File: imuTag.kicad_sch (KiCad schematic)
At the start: 29 parts, among them J1 Conn_02x05_Odd_Even, J2 Conn_01x05_Socket, J3 Conn_01x02_Pin, U1 E73-2G4M08S1C, U2 ME6211C30M5G-N, U3 GD25Q64ESIG, Y2 Crystal

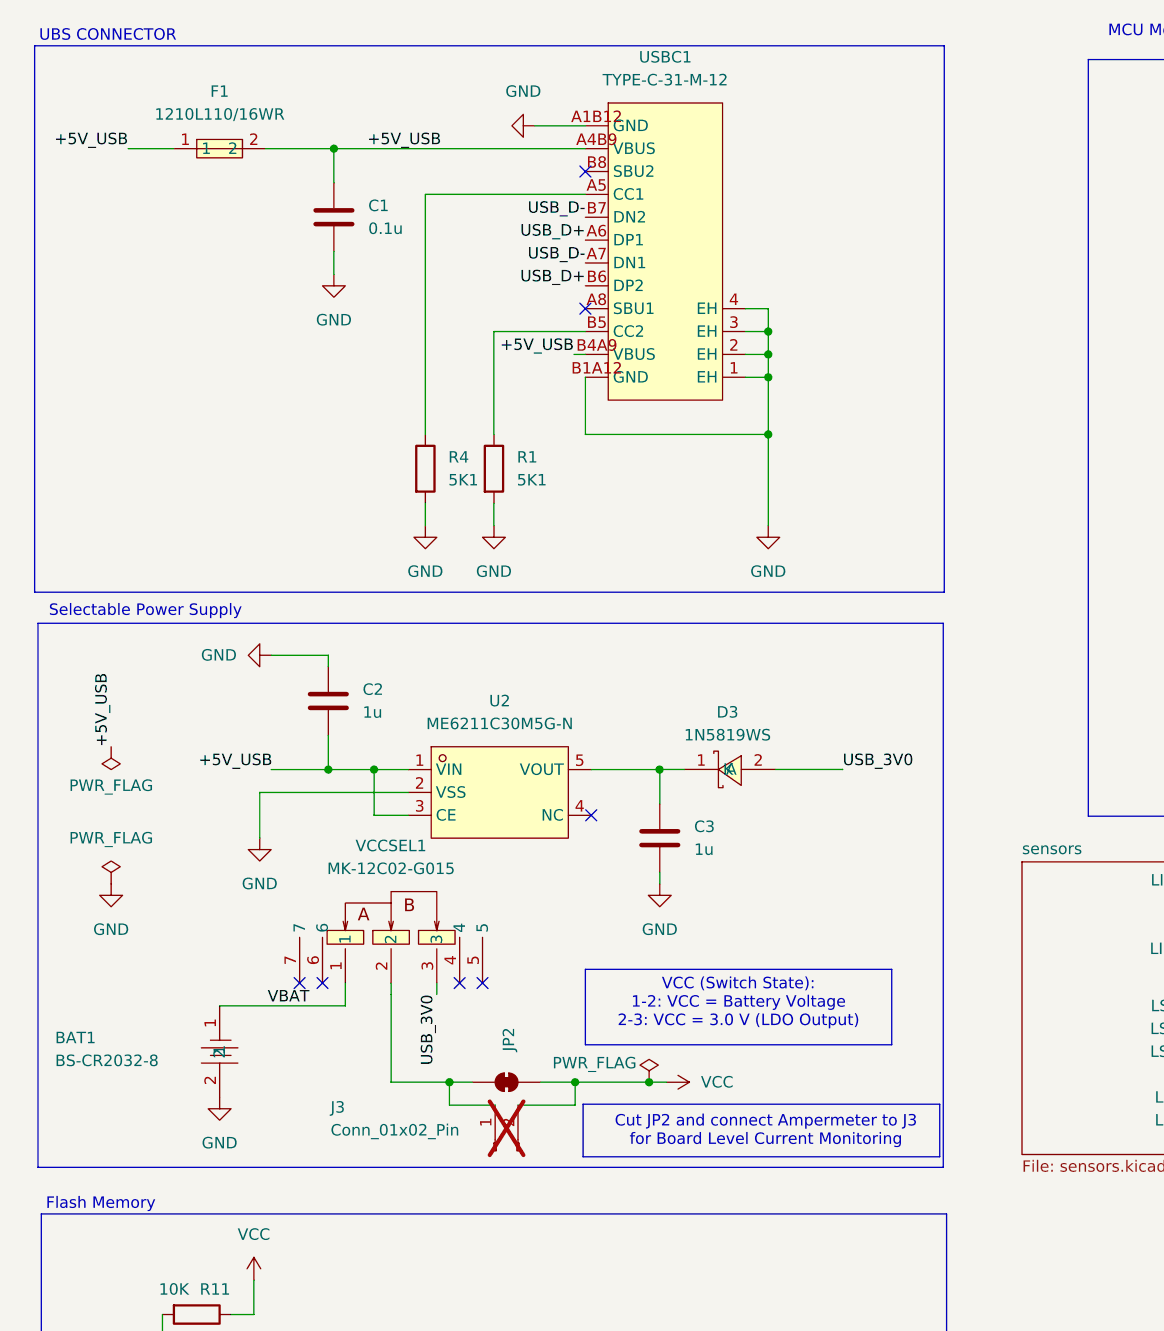
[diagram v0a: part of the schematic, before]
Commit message: Add copper zones before routing
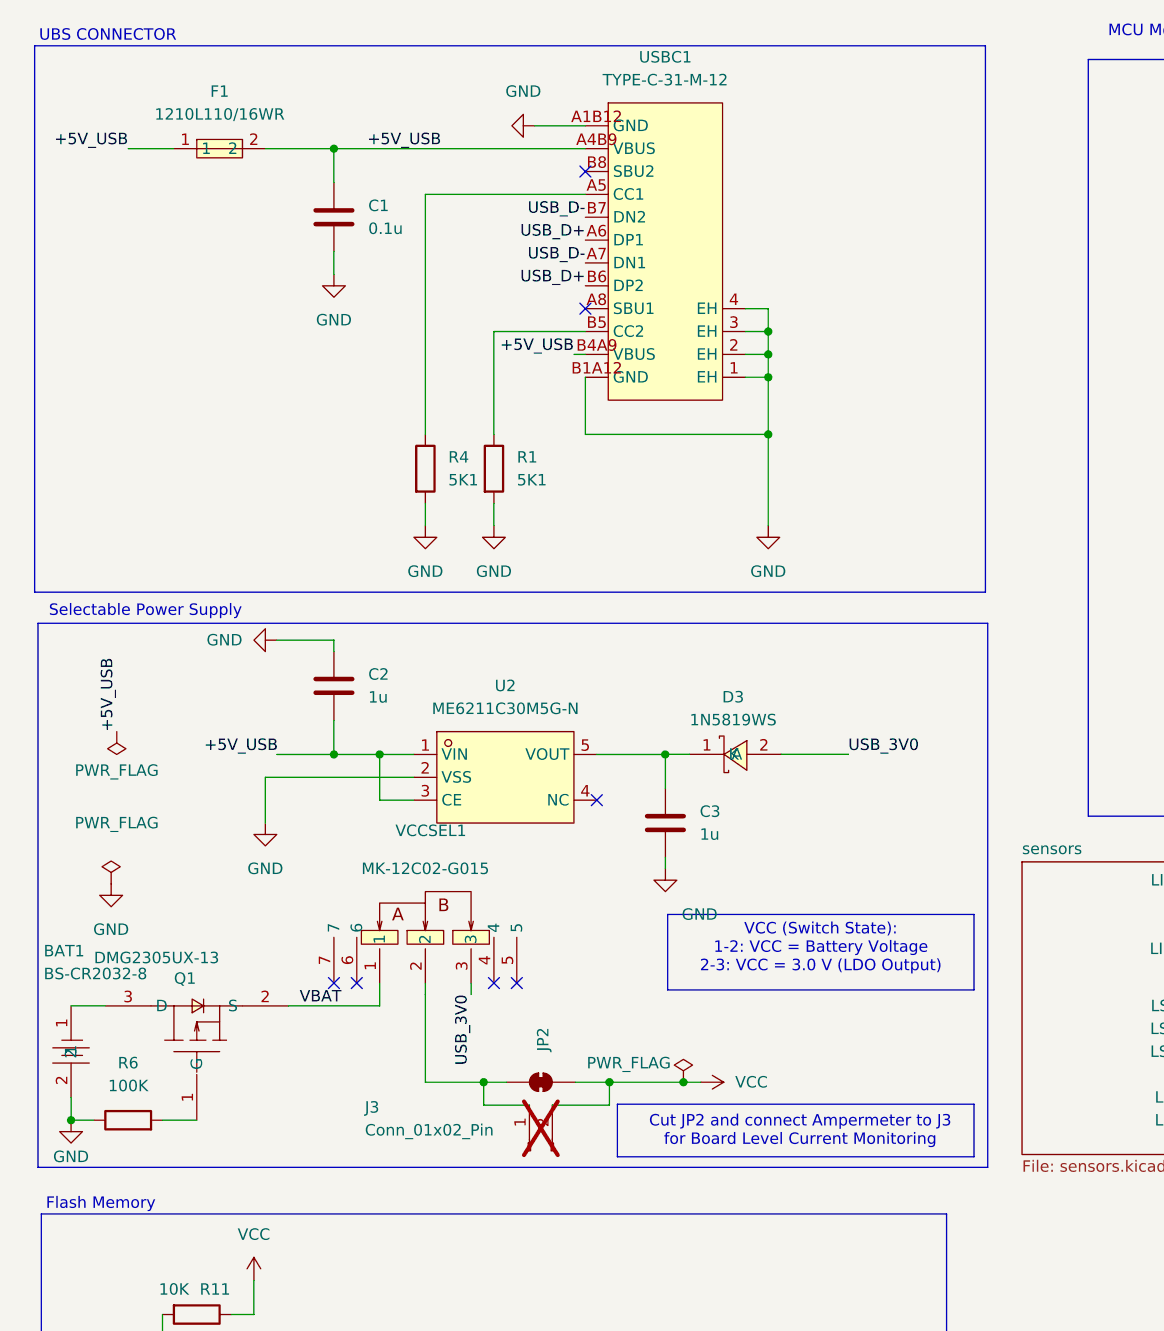
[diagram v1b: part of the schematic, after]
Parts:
- added Q1: DMG2305UX-13, EasyEDA:SOT-23-3_L2.9-W1.3-P1.90-LS2.4-BR, symbol EasyEDA:DMG2305UX-13
- added R6: 100K, Resistor_SMD:R_0603_1608Metric, symbol Device:R
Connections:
- net GND: now also R6.1
- net VBAT: now also Q1.2 (S); no longer BAT1.1
- new net: BAT1.1, Q1.3 (D)
- new net: Q1.1 (G), R6.2
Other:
- moved on the sheet: BAT1, C2, C3, D3, J3, JP2, U2, VCCSEL1

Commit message: Route power traces
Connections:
- net VBAT: now also BAT1.1, Q1.3 (D)
- net VCC: now also J3.1 (Pin_1), JP2.2 (B), VCCSEL1.2
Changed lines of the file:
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@@
+		)
+	)
+	(label "VCC"
+		(at 60.9612 127.7845 0)
+		(effects
+			(font
+				(size 1.27 1.27)
+			)
+			(justify left bottom)
 		)
 	)
@@
 		)
 	)
+	(label "VBAT"
+		(at 24.1094 124.46 0)
+		(effects
+			(font
+				(size 1.27 1.27)
+			)
+			(justify left bottom)
+		)
+	)

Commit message: Optimize power path component arrangement
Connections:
- net VBAT: no longer Q1.2 (S), VCCSEL1.1
- net VCC: no longer J3.1 (Pin_1), JP2.2 (B), VCCSEL1.2
- new net VBAT1: Q1.2 (S), VCCSEL1.1
- new net VCC_1: J3.1 (Pin_1), JP2.2 (B), VCCSEL1.2
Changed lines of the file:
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@@
+		)
+	)
+	(label "VBAT1"
+		(at 45.7982 124.46 0)
+		(effects
+			(font
+				(size 1.27 1.27)
+			)
+			(justify left bottom)
 		)
 	)
@@
 		)
 	)
-	(label "VBAT"
-		(at 46.99 124.46 0)
-		(effects
-			(font
-				(size 1.27 1.27)
-			)
-			(justify left bottom)
-		)
-	)
 	(label "SPI1_SCLK"
 		(at 180.34 34.29 180)
@@
 		)
 	)
-	(label "VCC"
+	(label "VCC_1"
 		(at 60.9612 127.7845 0)
 		(effects

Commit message: Routing of critical Paths, Finalizing Zones
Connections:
- net LIS2MDL_INT: now also U1.38 (P1.02); no longer U1.16 (P0.08)
- net LSM6DSV16_INT2: now also U1.16 (P0.08), U1.17 (P1.09); no longer U1.38 (P1.02)
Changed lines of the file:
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@@
-		)
-	)
-	(label "LSM6DSV16_INT2"
-		(at 240.03 33.02 0)
-		(effects
-			(font
-				(size 1.27 1.27)
-			)
-			(justify left bottom)
 		)
 	)
@@
 		)
 	)
+	(label "LIS2MDL_INT"
+		(at 240.03 33.02 0)
+		(effects
+			(font
+				(size 1.27 1.27)
+			)
+			(justify left bottom)
+		)
+	)
 	(label "USB_D-"
 		(at 240.03 55.88 0)
@@
 		)
 	)
+	(label "LSM6DSV16_INT2"
+		(at 203.2 69.85 270)
+		(effects
+			(font
+				(size 1.27 1.27)
+			)
+			(justify right bottom)
+		)
+	)
 	(label "AI4"
 		(at 189.23 121.92 180)
@@
 		)
 	)
+	(label "LSM6DSV16_INT2"
+		(at 205.74 69.85 270)
+		(effects
+			(font
+				(size 1.27 1.27)
+			)
+			(justify right bottom)
+		)
+	)
 	(label "SWDIO"
 		(at 240.03 35.56 0)
@@
 		)
 	)
-	(label "LIS2MDL_INT"
-		(at 203.2 69.85 270)
-		(effects
-			(font
-				(size 1.27 1.27)
-			)
-			(justify right bottom)
-		)
-	)

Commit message: draw Important Tracks
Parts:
- removed J2: Conn_01x05_Socket, Connector_PinSocket_2.54mm:PinSocket_1x05_P2.54mm_Vertical, symbol Connector:Conn_01x05_Socket
- C1, C14: footprint Capacitor_SMD:C_0603_1608Metric -> Capacitor_SMD:C_0402_1005Metric
- C4: footprint Capacitor_SMD:C_0603_1608Metric -> Capacitor_SMD:C_0603_1608Metric_Pad1.08x0.95mm_HandSolder
- R1, R11, R2, R3, R4, R5, R6: footprint Resistor_SMD:R_0603_1608Metric -> Resistor_SMD:R_0402_1005Metric
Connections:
- net AI0: no longer names the net of U1.7 (AI0)
- net AI4: no longer names the net of U1.4 (AI4)
- net AI5: no longer names the net of U1.8 (AI5)
- net AI6: no longer names the net of U1.10 (AI6)
- net AI7: no longer names the net of U1.9 (AI7)
- no-connect marks 17 -> 22
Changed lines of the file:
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@@
 	)
 	(no_connect
+		(at 180.34 54.61)
+	)
+	(no_connect
 		(at 240.03 20.32)
 	)
 	(no_connect
+		(at 180.34 46.99)
+	)
+	(no_connect
 		(at 193.04 69.85)
 	)
@@
 	)
 	(no_connect
+		(at 180.34 52.07)
+	)
+	(no_connect
 		(at 235.077 149.606)
 	)
@@
 	)
 	(no_connect
+		(at 180.34 49.53)
+	)
+	(no_connect
 		(at 80.01 101.6)
 	)
@@
 	)
 	(no_connect
+		(at 180.34 39.37)
+	)
+	(no_connect
 		(at 78.74 46.99)
 	)
@@
 		)
 	)
-	(label "AI5"
-		(at 189.23 124.46 180)
-		(effects
-			(font
-				(size 1.27 1.27)
-			)
-			(justify right bottom)
-		)
-	)
 	(label "VBAT1"
 		(at 45.7982 124.46 0)
@@
 		)
 	)
-	(label "AI6"
-		(at 189.23 127 180)
-		(effects
-			(font
-				(size 1.27 1.27)
-			)
-			(justify right bottom)
-		)
-	)
 	(label "LSM6DSV16_CS"
 		(at 180.34 36.83 180)
@@
 		)
 	)
-	(label "AI0"
-		(at 180.34 46.99 180)
-		(effects
-			(font
-				(size 1.27 1.27)
-			)
-			(justify right bottom)
-		)
-	)
 	(label "I2C0_SCL"
 		(at 240.03 22.86 0)
@@
 		)
 	)
-	(label "AI4"
-		(at 189.23 121.92 180)
-		(effects
-			(font
-				(size 1.27 1.27)
-			)
-			(justify right bottom)
-		)
-	)
 	(label "BATTERY_PIN"
 		(at 208.28 69.85 270)
@@
 		)
 	)
-	(label "AI7"
-		(at 180.34 52.07 180)
-		(effects
-			(font
-				(size 1.27 1.27)
-			)
-			(justify right bottom)
-		)
-	)
 	(label "LIS2MDL_CS"
 		(at 159.004 115.57 0)
@@
 		)
 	)
-	(label "AI7"
-		(at 189.23 129.54 180)
-		(effects
-			(font
-				(size 1.27 1.27)
-			)
-			(justify right bottom)
-		)
-	)
 	(label "SPI1_MOSI"
 		(at 180.34 31.75 180)
@@
 		)
 	)
-	(label "AI5"
-		(at 180.34 49.53 180)
-		(effects
-			(font
-				(size 1.27 1.27)
-			)
-			(justify right bottom)
-		)
-	)
 	(label "QSPI_IO2"
 		(at 43.18 175.26 180)
@@
 		)
 	)
-	(label "AI4"
-		(at 180.34 39.37 180)
-		(effects
-			(font
-				(size 1.27 1.27)
-			)
-			(justify right bottom)
-		)
-	)
-	(label "AI6"
-		(at 180.34 54.61 180)
-		(effects
-			(font
-				(size 1.27 1.27)
-			)
-			(justify right bottom)
-		)
-	)
 	(label "I2C0_SDA"
 		(at 240.03 27.94 0)
@@
 		)
 	)
-	(label "AI0"
-		(at 189.23 119.38 180)
-		(effects
-			(font
-				(size 1.27 1.27)
-			)
-			(justify right bottom)
-		)
-	)
 	(label "I2C0_SCL"
 		(at 159.004 113.03 0)
@@
 			)
 		)
-		(property "Footprint" "Resistor_SMD:R_0603_1608Metric"
+		(property "Footprint" "Resistor_SMD:R_0402_1005Metric"
 			(at 246.507 125.476 0)
 			(effects
@@
 			)
 		)
-		(property "Footprint" "Capacitor_SMD:C_0603_1608Metric"
+		(property "Footprint" "Capacitor_SMD:C_0603_1608Metric_Pad1.08x0.95mm_HandSolder"
 			(at 195.2752 95.25 0)
 			(effects
@@
 			)
 		)
-		(property "Footprint" "Resistor_SMD:R_0603_1608Metric"
+		(property "Footprint" "Resistor_SMD:R_0402_1005Metric"
 			(at 35.56 156.972 90)
 			(effects
@@
 			)
 		)
-		(property "Footprint" "Capacitor_SMD:C_0603_1608Metric"
+		(property "Footprint" "Capacitor_SMD:C_0402_1005Metric"
 			(at 99.3648 170.18 0)
 			(effects
@@
 			)
 		)
-		(property "Footprint" "Resistor_SMD:R_0603_1608Metric"
+		(property "Footprint" "Resistor_SMD:R_0402_1005Metric"
 			(at 228.219 117.221 0)
 			(effects
@@
 			)
 		)
-		(property "Footprint" "Resistor_SMD:R_0603_1608Metric"
+		(property "Footprint" "Resistor_SMD:R_0402_1005Metric"
 			(at 228.219 128.143 0)
 			(effects
@@
 			)
 		)
-		(property "Footprint" "Resistor_SMD:R_0603_1608Metric"
+		(property "Footprint" "Resistor_SMD:R_0402_1005Metric"
 			(at 59.182 64.77 90)
 			(effects
@@
 			)
 		)
-		(property "Footprint" "Capacitor_SMD:C_0603_1608Metric"
+		(property "Footprint" "Capacitor_SMD:C_0402_1005Metric"
 			(at 51.7652 40.64 0)
 			(effects
@@
 			)
 		)
-		(property "Footprint" "Resistor_SMD:R_0603_1608Metric"
+		(property "Footprint" "Resistor_SMD:R_0402_1005Metric"
 			(at 27.94 138.938 90)
 			(effects
@@
 			)
 		)
-		(property "Footprint" "Resistor_SMD:R_0603_1608Metric"
+		(property "Footprint" "Resistor_SMD:R_0402_1005Metric"
 			(at 66.802 64.77 90)
 			(effects
@@
 					(unit 1)
 				)
-			)
-		)
-	)
-	(symbol
-		(lib_id "Connector:Conn_01x05_Socket")
-		(at 194.31 124.46 0)
-		(unit 1)
-		(exclude_from_sim no)
-		(in_bom yes)
-		(on_board yes)
-		(dnp yes)
-		(property "Reference" "J2"
-			(at 186.182 111.76 0)
-			(effects
-				(font
-					(size 1.27 1.27)
-				)
-				(justify left)
-			)
-		)
-		(property "Value" "Conn_01x05_Socket"
-			(at 186.182 114.3 0)
-			(effects
-				(font
-					(size 1.27 1.27)
-				)
-				(justify left)
-			)
-		)
-		(property "Footprint" "Connector_PinSocket_2.54mm:PinSocket_1x05_P2.54mm_Vertical"
-			(at 194.31 124.46 0)
-			(effects
-				(font
-					(size 1.27 1.27)
-				)
-				(hide yes)
-			)
-		)
-		(property "Datasheet" "~"
-			(at 194.31 124.46 0)
-			(effects
-				(font
-					(size 1.27 1.27)
-				)
-				(hide yes)
-			)
-		)
-		(property "Description" "Generic connector, single row, 01x05, script generated"
-			(at 194.31 124.46 0)
-			(effects
-				(font
-					(size 1.27 1.27)
-				)
-				(hide yes)
-			)
-		)
-		(pin "2"
-		)
-		(pin "1"
-		)
-		(pin "3"
-		)
-		(pin "4"
-		)
-		(pin "5"
-		)
-		(instances
-			(project ""
-				(path "/b0790ebf-2d8c-4cec-b4ed-465f5b1bb1fd"
-					(reference "J2")
-					(unit 1)
-				)

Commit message: Finalize PCB for production
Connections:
- net +5V_USB: no longer C1.1, F1.2, USBC1.A4B9 (VBUS)
- new net +5V_USB_prot: C1.1, F1.2, USBC1.A4B9 (VBUS)
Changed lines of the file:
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@@
 		)
 	)
-	(label "+5V_USB"
+	(label "+5V_USB_prot"
 		(at 62.7201 29.21 180)
 		(effects

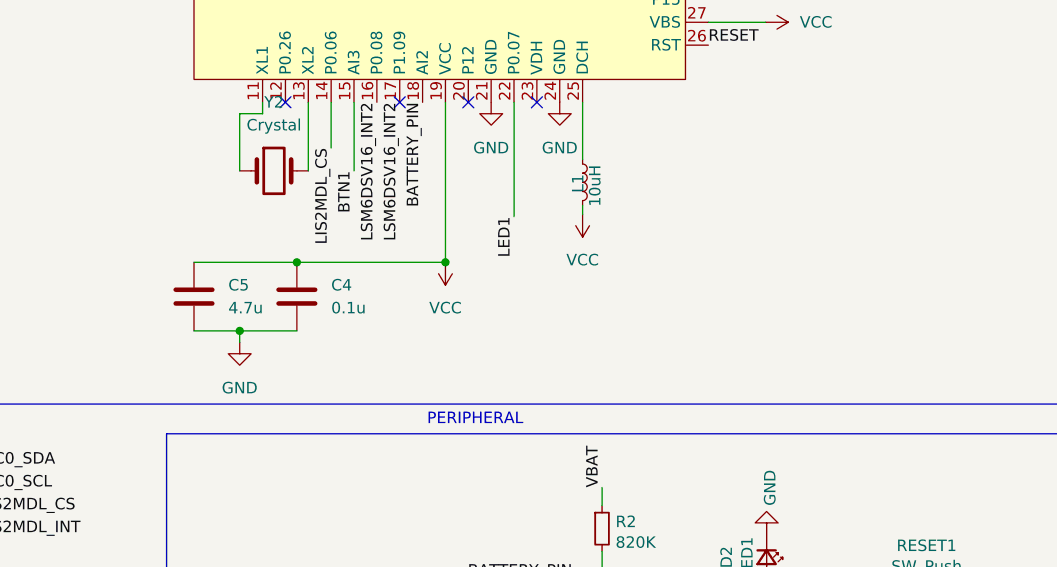
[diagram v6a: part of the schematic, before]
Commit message: Add 32 kHz crystal and load capacitors
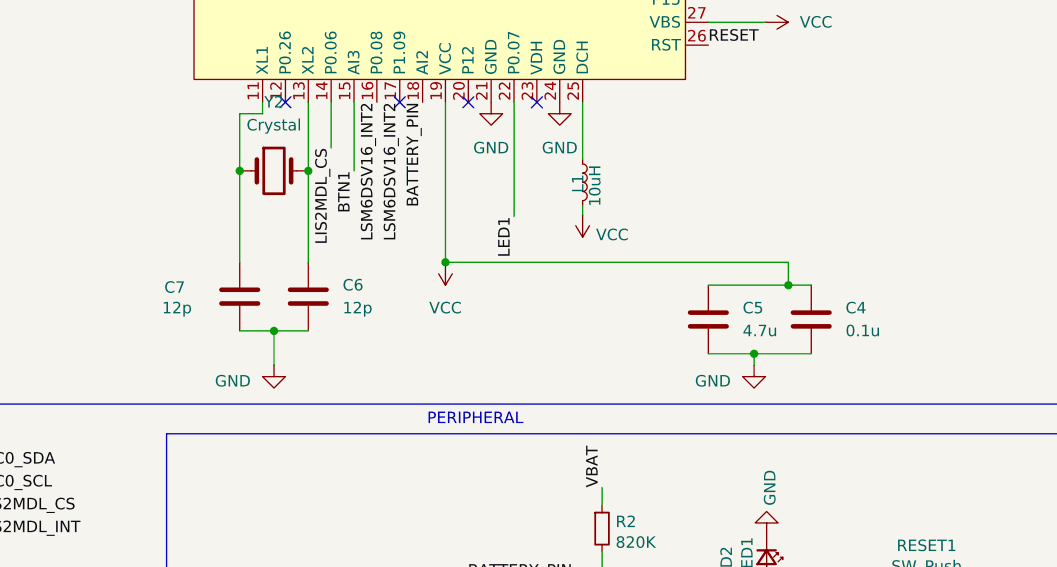
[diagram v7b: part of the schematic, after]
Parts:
- added C6, C7: 12p, Capacitor_SMD:C_0402_1005Metric, symbol Device:C
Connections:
- net GND: now also C6.2, C7.2
- net at U1.11 (XL1), Y2.1: now also C7.1
- net at U1.13 (XL2), Y2.2: now also C6.1
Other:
- moved on the sheet: C4, C5
